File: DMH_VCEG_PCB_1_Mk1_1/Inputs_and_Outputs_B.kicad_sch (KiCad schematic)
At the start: 44 parts, among them J11 TS_Jack_6.35mm_Sw, J12 TS_Jack_6.35mm_Sw, J13 TS_Jack_6.35mm_Sw, J14 TS_Jack_6.35mm_Sw, J15 TS_Jack_6.35mm_Sw, J16 TS_Jack_6.35mm_Sw, J17 TS_Jack_6.35mm_Sw, J18 TS_Jack_6.35mm_Sw, J19 TS_Jack_6.35mm_Sw, J20 TS_Jack_6.35mm_Sw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

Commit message: Out R rework ongoing
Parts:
- R11: value 100k -> 68k
- R18: value 68k -> 100k
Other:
- note removed: "Must be inverted"
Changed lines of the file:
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@@
 	)
 	(rectangle
-		(start 116.84 187.96)
-		(end 134.62 193.04)
-		(stroke
-			(width 0)
-			(type default)
-		)
-		(fill
-			(type none)
-		)
-	)
-	(rectangle
 		(start 72.39 13.97)
 		(end 152.4 148.59)
@@
 		)
 	)
-	(text "Must be inverted"
-		(exclude_from_sim no)
-		(at 126.746 186.69 0)
-		(effects
-			(font
-				(size 1.27 1.27)
-			)
-		)
-	)
 	(text "PCB 2"
 		(exclude_from_sim no)
@@
 			)
 		)
-		(property "Value" "68k"
+		(property "Value" "100k"
 			(at 130.81 194.31 90)
 			(effects
@@
 			)
 		)
-		(property "Value" "100k"
+		(property "Value" "68k"
 			(at 120.65 194.31 90)
 			(effects

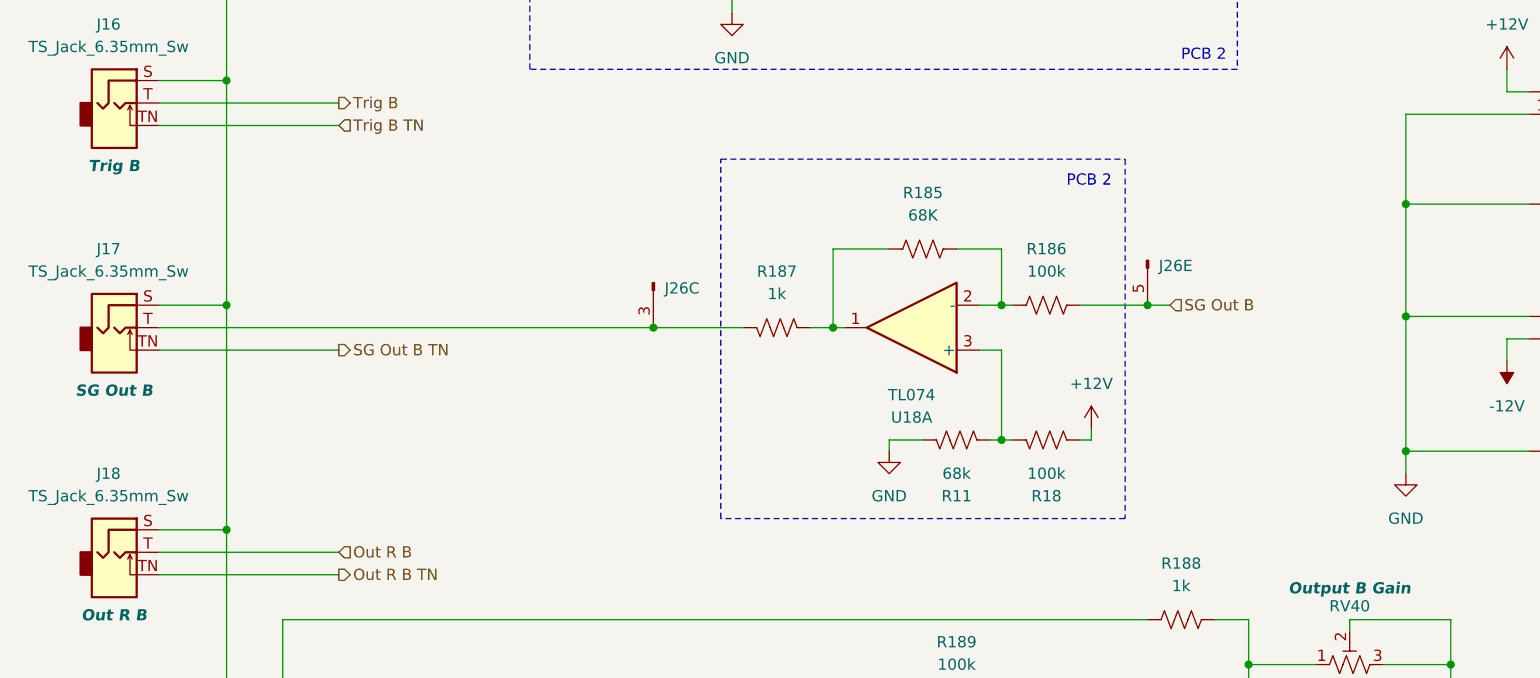
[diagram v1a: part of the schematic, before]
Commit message: Added diodes to Sustain Gate outputs
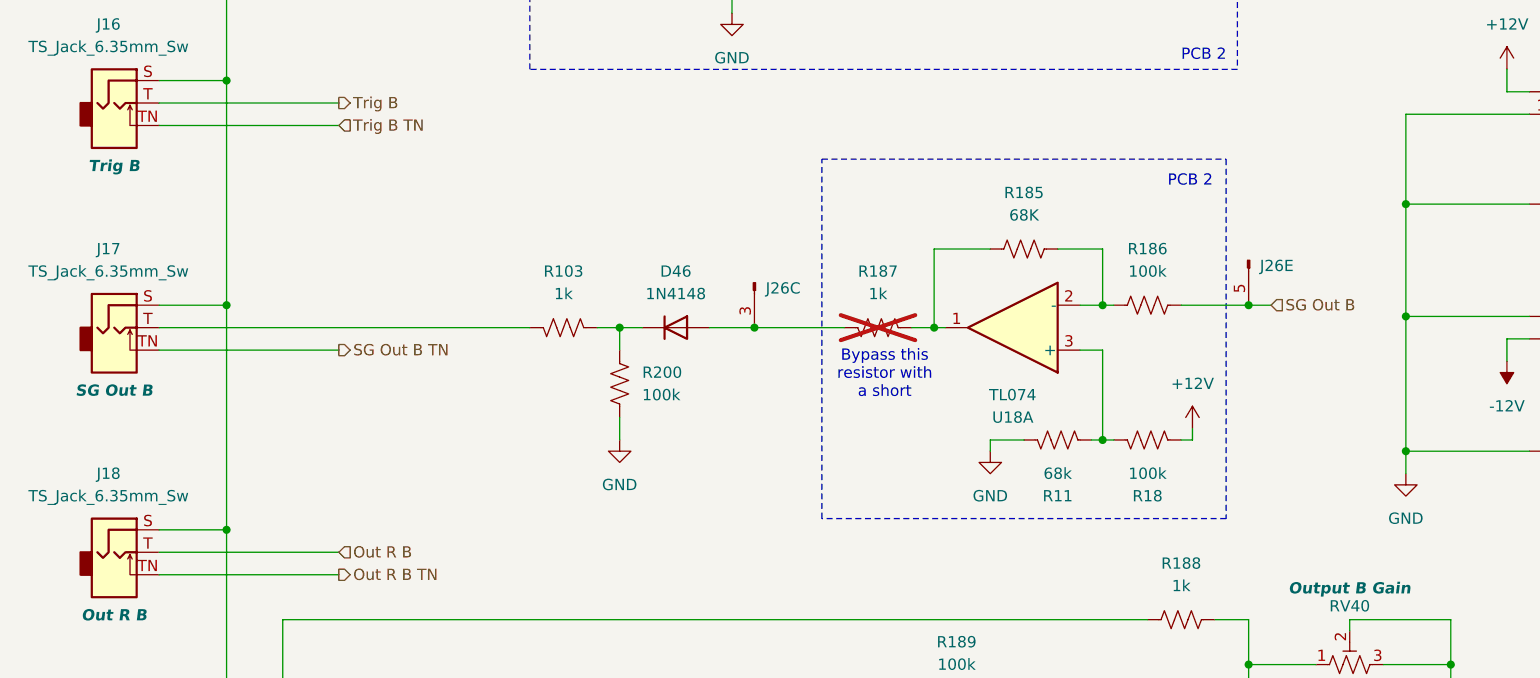
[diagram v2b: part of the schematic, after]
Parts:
- added D46: 1N4148, Diode_THT:D_DO-35_SOD27_P7.62mm_Horizontal, symbol Diode:1N4148
- added R103: 1k, Resistor_THT:R_Axial_DIN0207_L6.3mm_D2.5mm_P7.62mm_Horizontal, symbol Device:R_US
- added R200: 100k, Resistor_THT:R_Axial_DIN0207_L6.3mm_D2.5mm_P7.62mm_Horizontal, symbol Device:R_US
- R187: now not fitted
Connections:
- net GND: now also R200.2
- net at J26.3 (Pin_3), R187.1: now also D46.2 (A); no longer J17.T
- new net: D46.1 (K), R103.2, R200.1
- new net: J17.T, R103.1
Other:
- note added: "Bypass this resistor with a short"
- moved on the sheet: J26C, J26E, R11, R18, R185, R186, U18A
